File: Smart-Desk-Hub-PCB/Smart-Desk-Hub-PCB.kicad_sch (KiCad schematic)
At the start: 5 parts, among them U1 ESP32-S3-WROOM-1, U2 MAX98357A, U3 BME280, U4 CH343G

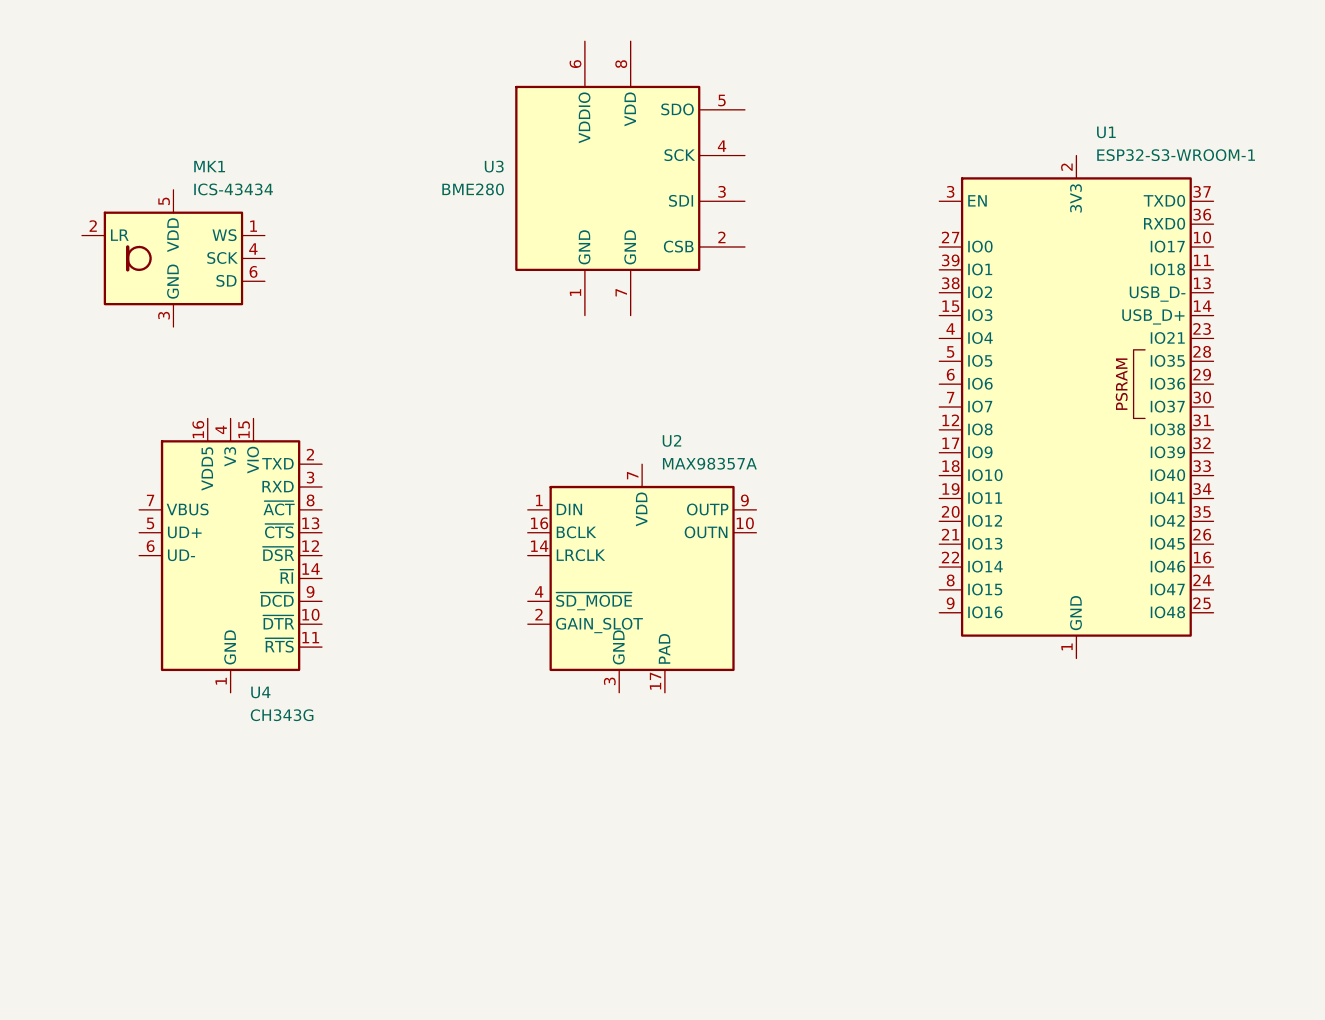
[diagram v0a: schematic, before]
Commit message: Finalize PCB schematic and components list, begin PCB layout
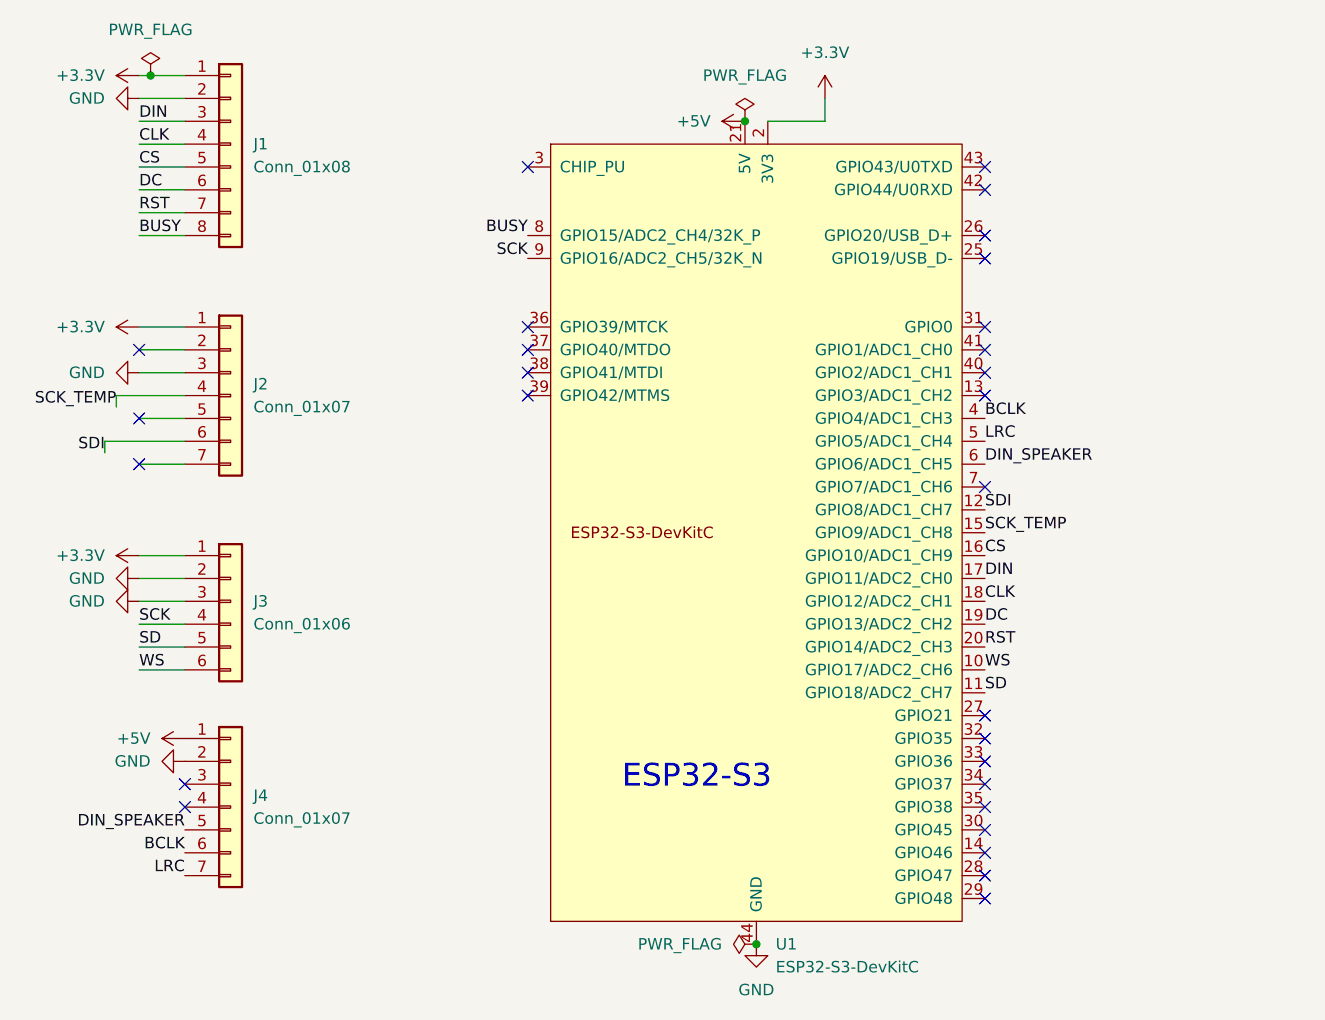
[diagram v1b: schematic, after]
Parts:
- removed MK1: ICS-43434, Sensor_Audio:InvenSense_ICS-43434-6_3.5x2.65mm, symbol Sensor_Audio:ICS-43434
- removed U1: ESP32-S3-WROOM-1, RF_Module:ESP32-S3-WROOM-1, symbol RF_Module:ESP32-S3-WROOM-1
- removed U2: MAX98357A, Package_DFN_QFN:TQFN-16-1EP_3x3mm_P0.5mm_EP1.23x1.23mm, symbol Audio:MAX98357A
- removed U3: BME280, Package_LGA:Bosch_LGA-8_2.5x2.5mm_P0.65mm_ClockwisePinNumbering, symbol Sensor:BME280
- removed U4: CH343G, Package_SO:SOIC-16_3.9x9.9mm_P1.27mm, symbol Interface_USB:CH343G
- added J1: Conn_01x08, Connector_PinHeader_2.54mm:PinHeader_1x08_P2.54mm_Vertical, symbol Connector_Generic:Conn_01x08
- added J2, J4: Conn_01x07, Connector_PinHeader_2.54mm:PinHeader_1x07_P2.54mm_Vertical, symbol Connector_Generic:Conn_01x07
- added J3: Conn_01x06, Connector_PinHeader_2.54mm:PinHeader_1x06_P2.54mm_Vertical, symbol Connector_Generic:Conn_01x06
- added U1: ESP32-S3-DevKitC, PCM_Espressif:ESP32-S3-DevKitC, symbol PCM_Espressif:ESP32-S3-DevKitC
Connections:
- new net +3.3V: J1.1 (Pin_1), J2.1 (Pin_1), J3.1 (Pin_1), U1.1 (3V3), U1.2 (3V3)
- new net +5V: J4.1 (Pin_1), U1.21 (5V)
- new net BCLK: J4.6 (Pin_6), U1.4 (GPIO4/ADC1_CH3)
- new net BUSY: J1.8 (Pin_8), U1.8 (GPIO15/ADC2_CH4/32K_P)
- new net CLK: J1.4 (Pin_4), U1.18 (GPIO12/ADC2_CH1)
- new net CS: J1.5 (Pin_5), U1.16 (GPIO10/ADC1_CH9)
- new net DC: J1.6 (Pin_6), U1.19 (GPIO13/ADC2_CH2)
- new net DIN: J1.3 (Pin_3), U1.17 (GPIO11/ADC2_CH0)
- new net DIN_SPEAKER: J4.5 (Pin_5), U1.6 (GPIO6/ADC1_CH5)
- new net GND: J1.2 (Pin_2), J2.3 (Pin_3), J3.2 (Pin_2), J3.3 (Pin_3), J4.2 (Pin_2), U1.22 (GND), U1.23 (GND), U1.24 (GND), U1.44 (GND)
- new net LRC: J4.7 (Pin_7), U1.5 (GPIO5/ADC1_CH4)
- new net RST: J1.7 (Pin_7), U1.20 (GPIO14/ADC2_CH3)
- new net SCK: J3.4 (Pin_4), U1.9 (GPIO16/ADC2_CH5/32K_N)
- new net SCK_TEMP: J2.4 (Pin_4), U1.15 (GPIO9/ADC1_CH8)
- new net SD: J3.5 (Pin_5), U1.11 (GPIO18/ADC2_CH7)
- new net SDI: J2.6 (Pin_6), U1.12 (GPIO8/ADC1_CH7)
- new net WS: J3.6 (Pin_6), U1.10 (GPIO17/ADC2_CH6)
- no-connect marks 0 -> 28
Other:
- note added: "ESP32-S3"

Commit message: Fix PCB dimensions, add decoupling capacitors, and update Components list and README
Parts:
- added C1, C2: 10 µF, Capacitor_SMD:C_0805_2012Metric_Pad1.18x1.45mm_HandSolder, symbol Device:C
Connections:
- net +3.3V: now also C2.1
- net +5V: now also C1.1
- net GND: now also C1.2, C2.2
- net SCK_TEMP: now also U1.28 (GPIO47); no longer U1.15 (GPIO9/ADC1_CH8)
- net SDI: now also U1.29 (GPIO48); no longer U1.12 (GPIO8/ADC1_CH7)
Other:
- note added: "10/16/2026"
- note added: "2"
- note added: "PCB Design for the Smart Desk Hub - Version 2"
- note added: "PCB Schematic for the Smart Desk Hub Project"
- moved on the sheet: J1, J2, J3, J4, U1
